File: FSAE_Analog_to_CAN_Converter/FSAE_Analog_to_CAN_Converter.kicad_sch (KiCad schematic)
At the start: 0 parts

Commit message: placed components in schematic, four devices, STM32, CAN_Transciever, 12 to 3.3 V Buck converter, 5 block connector
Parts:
- added J1: Conn_01x05_Pin, symbol Connector:Conn_01x05_Pin
- added U1: STM32F103RCTx, Package_QFP:LQFP-64_10x10mm_P0.5mm, symbol MCU_ST_STM32F1:STM32F103RCTx
- added U2: XL1509-3.3, Package_SO:SOIC-8_3.9x4.9mm_P1.27mm, symbol Regulator_Switching:XL1509-3.3
- added U3: MCP2561-E-MF, Package_DFN_QFN:DFN-8-1EP_3x3mm_P0.65mm_EP1.55x2.4mm, symbol Interface_CAN_LIN:MCP2561-E-MF
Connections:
- new net: U1.18 (VSS), U1.31 (VSS), U1.47 (VSS), U1.63 (VSS)
- new net: U3.2 (VSS), U3.9 (VSS)
- new net: U2.5 (GND), U2.6 (GND), U2.7 (GND), U2.8 (GND)

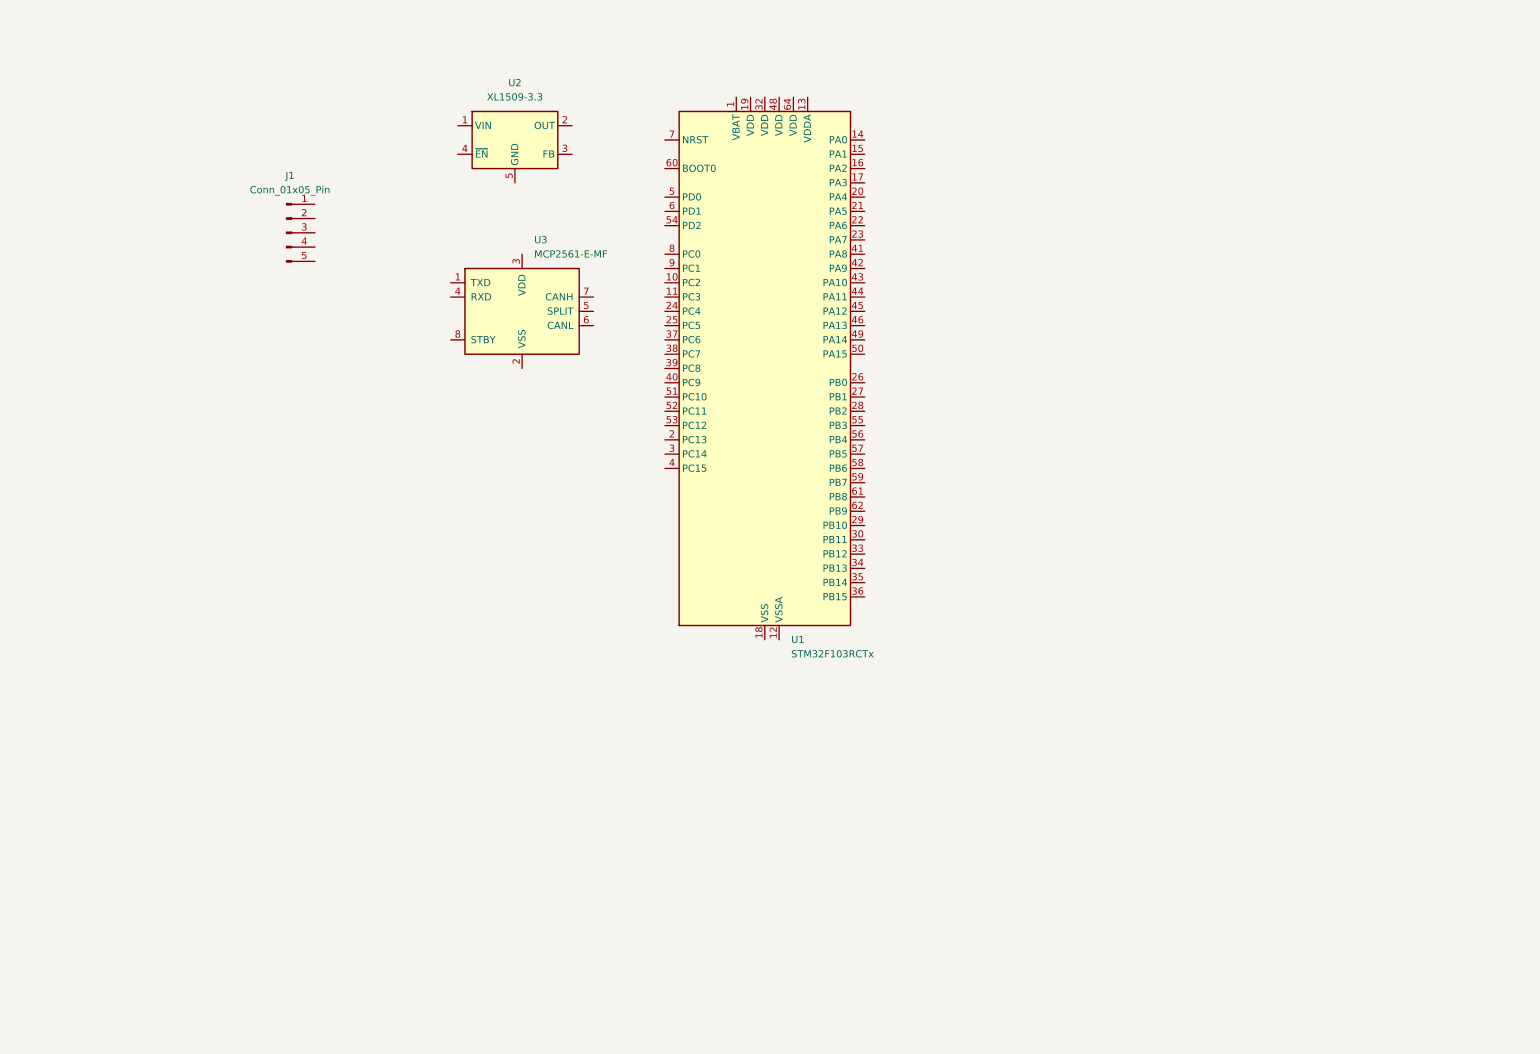
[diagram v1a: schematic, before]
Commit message: 12.0 to 3.3 V Buck converter stepdown
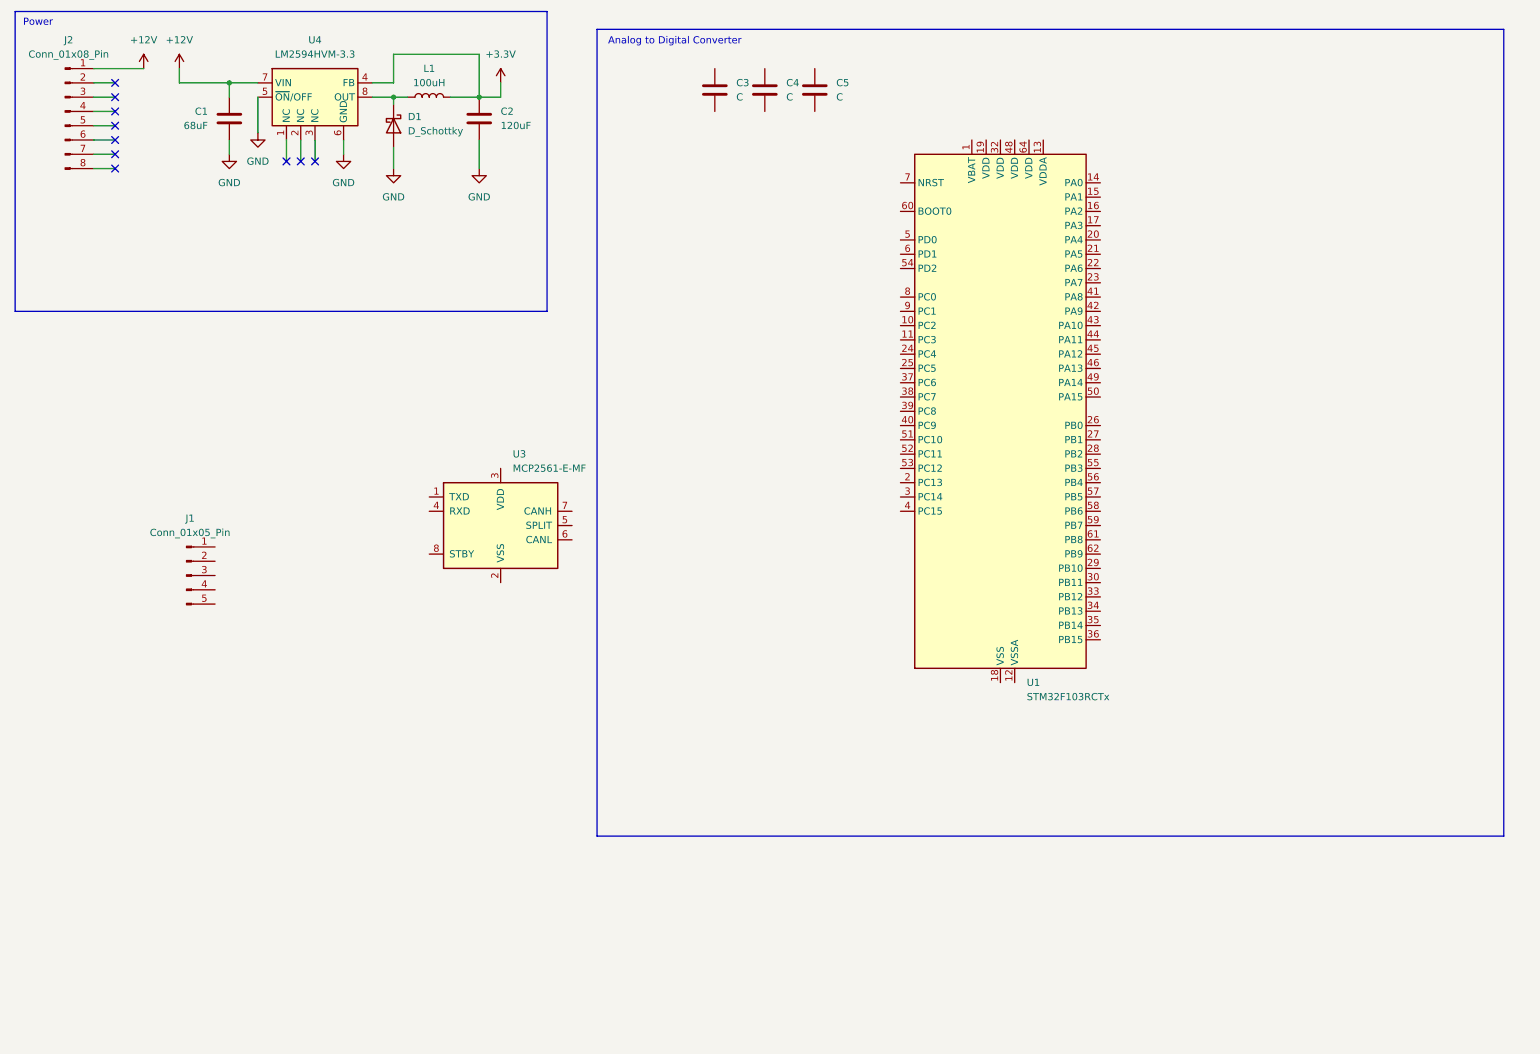
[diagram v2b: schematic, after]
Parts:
- removed U2: XL1509-3.3, Package_SO:SOIC-8_3.9x4.9mm_P1.27mm, symbol Regulator_Switching:XL1509-3.3
- added C1: 68uF, symbol Device:C
- added C2: 120uF, symbol Device:C
- added C3, C4, C5: C, symbol Device:C
- added D1: D_Schottky, symbol Device:D_Schottky
- added J2: Conn_01x08_Pin, symbol Connector:Conn_01x08_Pin
- added L1: 100uH, symbol Device:L
- added U4: LM2594HVM-3.3, Package_SO:SOIC-8_3.9x4.9mm_P1.27mm, symbol Regulator_Switching:LM2594HVM-3.3
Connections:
- new net: D1.1 (K), L1.1, U4.8 (OUT)
- new net +12V: C1.1, J2.1 (Pin_1), U4.7 (VIN)
- new net +3.3V: C2.1, L1.2, U4.4 (FB)
- new net GND: C1.2, C2.2, D1.2 (A), U4.5 (~{ON}/OFF), U4.6 (GND)
- no-connect marks 0 -> 10
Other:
- note added: "Analog to Digital Converter"
- note added: "Power"
- moved on the sheet: J1, U1, U3

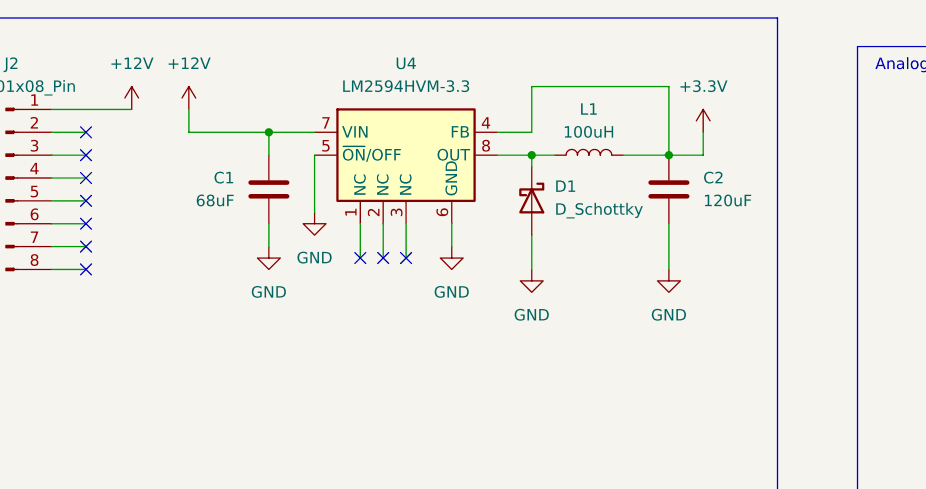
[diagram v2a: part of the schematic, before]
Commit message: new parts, can transciever and ldo
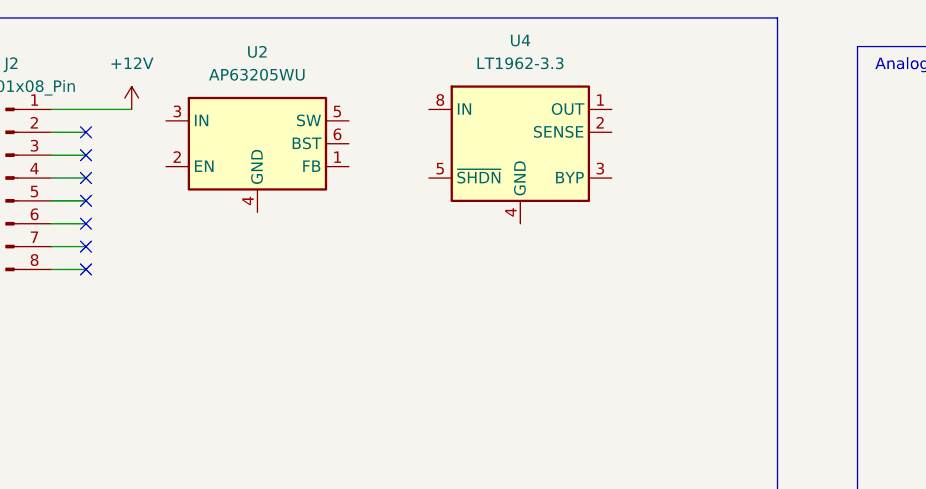
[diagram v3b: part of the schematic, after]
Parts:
- removed C1: 68uF, symbol Device:C
- removed C2: 120uF, symbol Device:C
- removed D1: D_Schottky, symbol Device:D_Schottky
- removed L1: 100uH, symbol Device:L
- removed U4: LM2594HVM-3.3, Package_SO:SOIC-8_3.9x4.9mm_P1.27mm, symbol Regulator_Switching:LM2594HVM-3.3
- added U2: AP63205WU, Package_TO_SOT_SMD:TSOT-23-6, symbol Regulator_Switching:AP63205WU
- added U4: LT1962-3.3, Package_SO:MSOP-8_3x3mm_P0.65mm, symbol Regulator_Linear:LT1962-3.3
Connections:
- no-connect marks 10 -> 7

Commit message: finished power section
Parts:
- added C1, C11: 10uF, symbol Device:C
- added C10: 0.01uF, symbol Device:C
- added C2: 100nF, symbol Device:C
- added C6: 100pF, symbol Device:C
- added C7, C9: 22uF, symbol Device:C
- added C8: 1uF, symbol Device:C
- added L1: 10uH, symbol Device:L
- added R1: 157k, symbol Device:R
- added R2: 30k, symbol Device:R
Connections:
- net +12V: now also U2.2 (EN), U2.3 (IN), C1.1
- net at U2.1 (FB): now also C6.2, R1.2, R2.1
- net GND: now reaches U2.4 (GND)
- net GND: now also U4.4 (GND), C1.2, C11.1, C7.2, C8.2, C9.2, R2.2
- net at U2.5 (SW): now also C2.1, L1.1
- net at U2.6 (BST): now also C2.2
- net +3.3V: now reaches U4.1 (OUT)
- net +3.3V: now also U4.2 (SENSE), C10.2, C11.2
- net at U4.3 (BYP): now also C10.1
- net +5V: now reaches U4.5 (~{SHDN})
- net +5V: now also U4.8 (IN), C6.1, C7.1, C8.1, C9.1, L1.2, R1.1
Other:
- moved on the sheet: C3, C4, C5, J1, U1, U2, U4

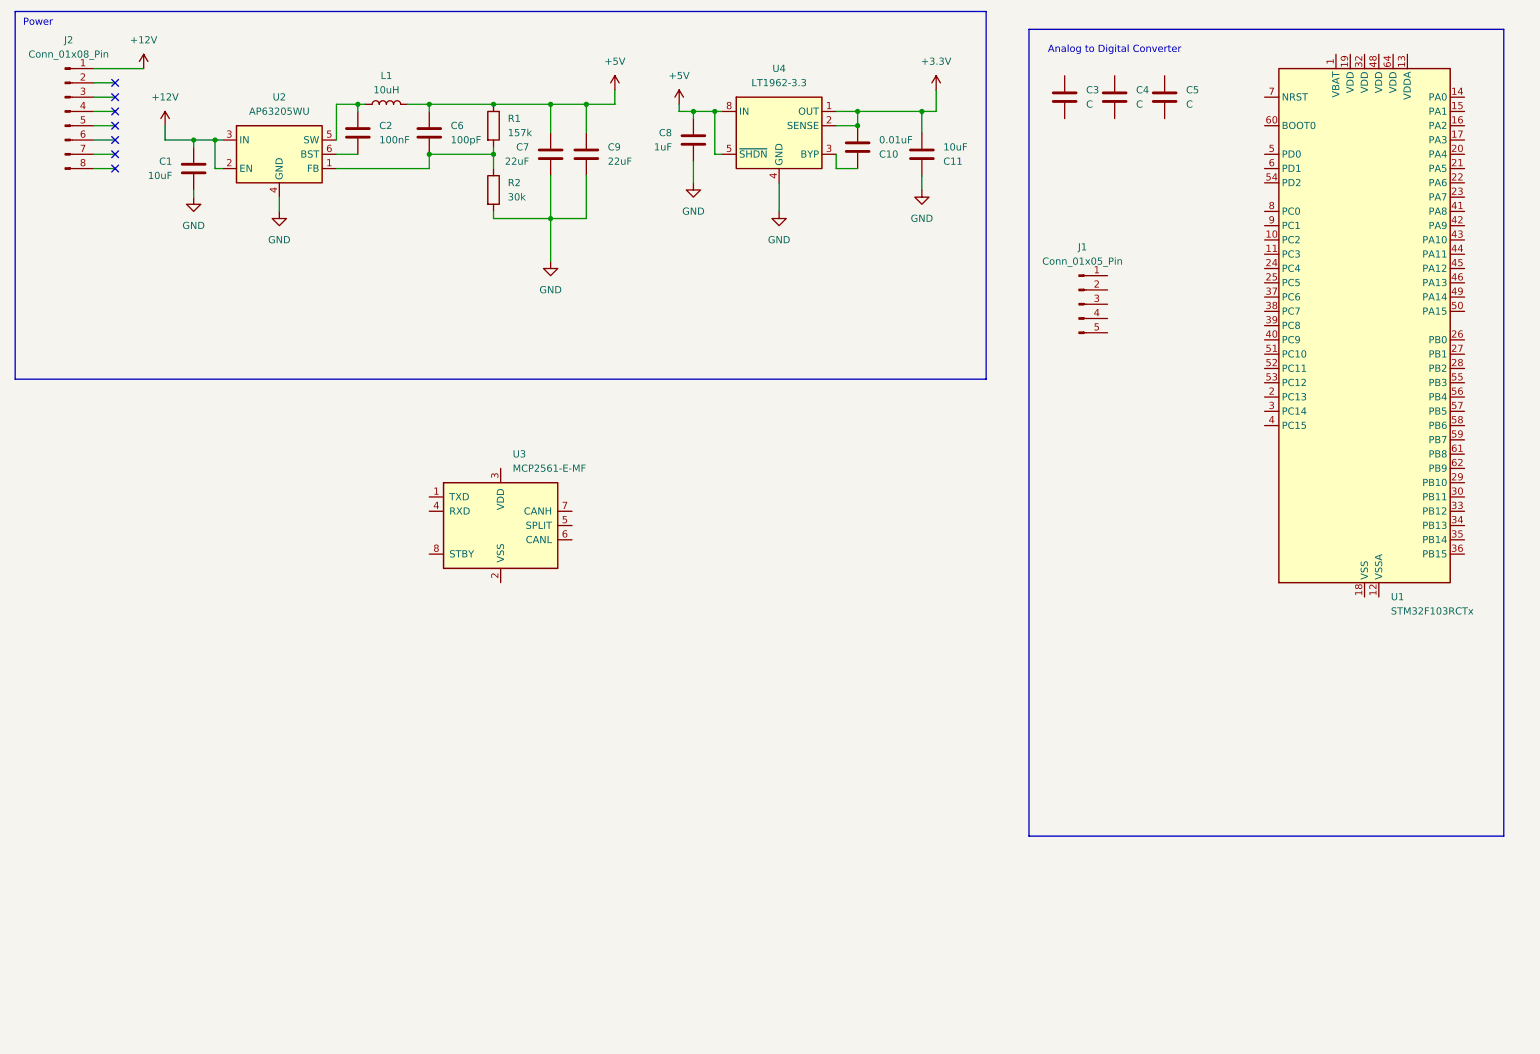
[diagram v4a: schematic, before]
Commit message: ostensibly finished schematic. I need to add a 5 V LDO, and a external oscillator
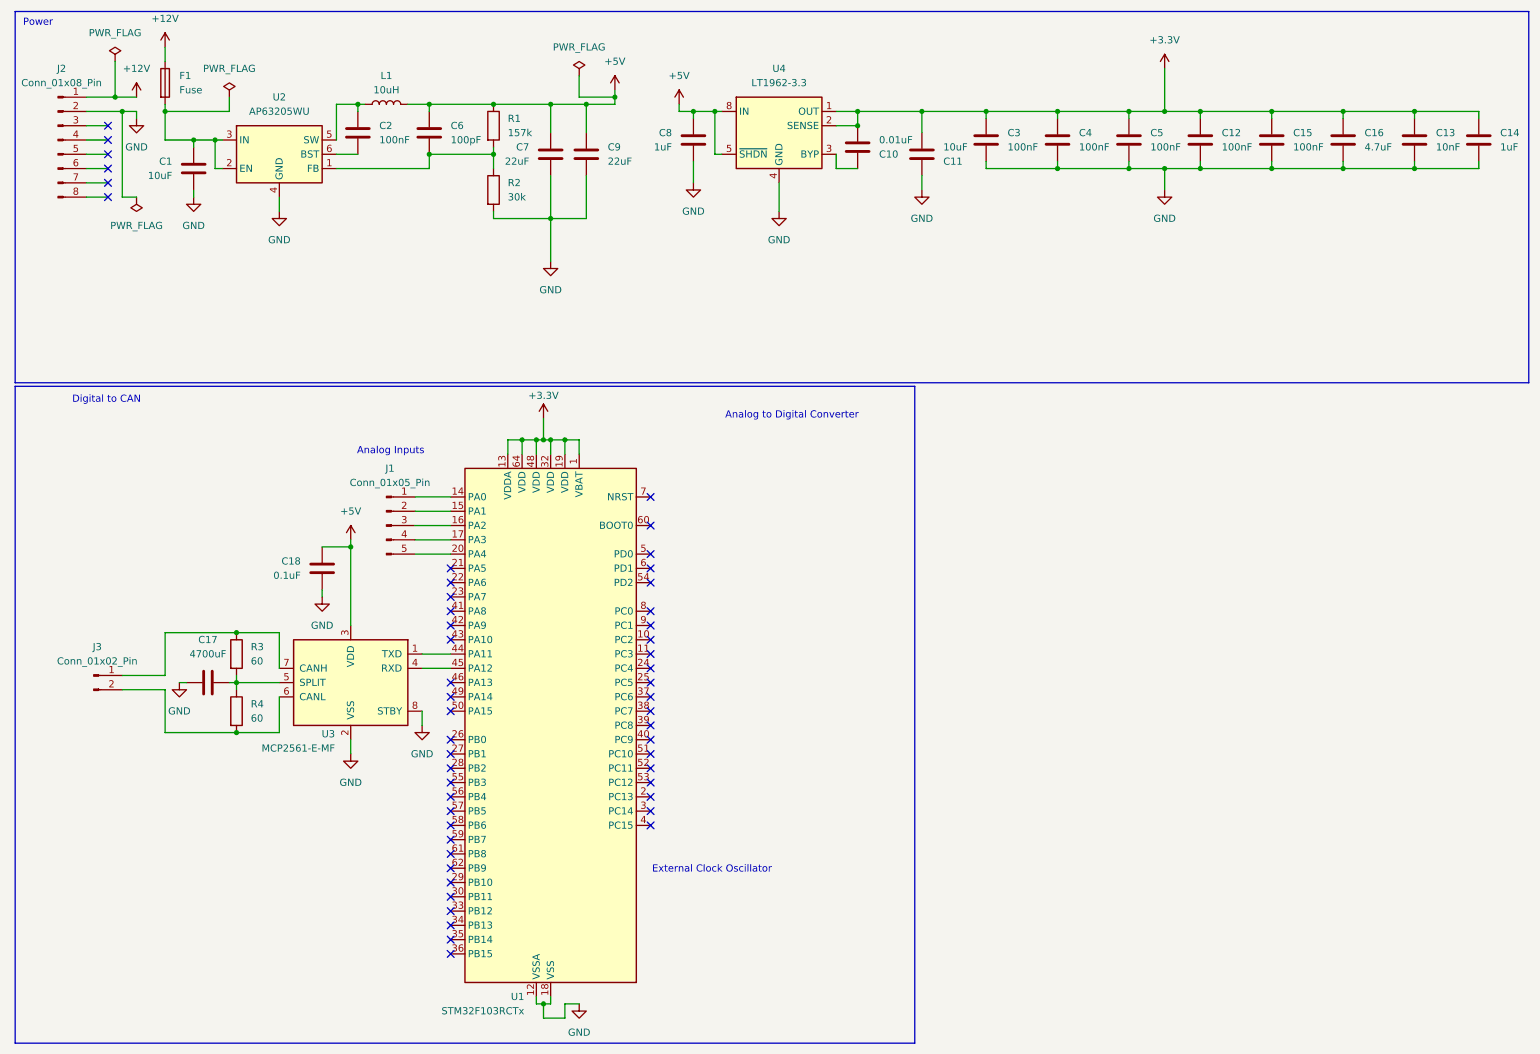
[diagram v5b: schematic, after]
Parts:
- added C12, C15: 100nF, symbol Device:C
- added C13: 10nF, symbol Device:C
- added C14: 1uF, symbol Device:C
- added C16: 4.7uF, symbol Device:C
- added C17: 4700uF, symbol Device:C
- added C18: 0.1uF, symbol Device:C
- added F1: Fuse, symbol Device:Fuse
- added J3: Conn_01x02_Pin, symbol Connector:Conn_01x02_Pin
- added R3, R4: 60, symbol Device:R
- C3, C4, C5: value C -> 100nF
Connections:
- net +12V: now also F1.1; no longer C1.1, U2.2 (EN), U2.3 (IN)
- net +3.3V: now also C3.1, C4.1, C5.1, U1.1 (VBAT), U1.13 (VDDA), U1.19 (VDD), U1.32 (VDD), U1.48 (VDD), U1.64 (VDD), C12.1, C13.1, C14.1, C15.1, C16.1
- net +5V: now also U3.3 (VDD), C18.2
- net GND: now also C3.2, C4.2, C5.2, J2.2 (Pin_2), U1.12 (VSSA), U1.18 (VSS), U1.31 (VSS), U1.47 (VSS), U1.63 (VSS), U3.2 (VSS), U3.8 (STBY), U3.9 (VSS), C12.2, C13.2, C14.2, C15.2, C16.2, C17.1, C18.1
- net at U1.14 (PA0): now also J1.1 (Pin_1)
- net at U1.15 (PA1): now also J1.2 (Pin_2)
- net at U1.16 (PA2): now also J1.3 (Pin_3)
- net at U1.17 (PA3): now also J1.4 (Pin_4)
- net at U1.20 (PA4): now also J1.5 (Pin_5)
- net at U1.44 (PA11): now also U3.1 (TXD)
- net at U1.45 (PA12): now also U3.4 (RXD)
- net at U3.5 (SPLIT): now also C17.2, R3.2, R4.1
- net at U3.6 (CANL): now also J3.2 (Pin_2), R4.2
- net at U3.7 (CANH): now also J3.1 (Pin_1), R3.1
- new net: C1.1, F1.2, U2.2 (EN), U2.3 (IN)
- no-connect marks 7 -> 52
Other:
- note added: "Analog Inputs"
- note added: "Digital to CAN"
- note added: "External Clock Oscillator"
- moved on the sheet: C3, C4, J1, J2, U1, U3

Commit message: check
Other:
- note added: "Analog to CAN Converter"
- note removed: "Analog to Digital Converter"
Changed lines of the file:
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@@
 		)
 	)
-	(text "Analog to Digital Converter\n"
+	(text "Analog to CAN Converter\n"
 		(exclude_from_sim no)
 		(at 153.416 85.852 0)
